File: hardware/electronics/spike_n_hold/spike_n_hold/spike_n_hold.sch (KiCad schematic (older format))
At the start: 132 parts, among them J1 input_trigger_2, J10 input_trigger_6, J11 input_trigger_5, J12 to_solenoid_6, J13 to_solenoid_5, J2 input_trigger_1, J3 to_solenoid_2, J4 to_solenoid_1, J5 input_trigger_4, J6 input_trigger_3, J7 to_solenoid_4, J8 to_solenoid_3, J9 Barrel_Jack_MountingPin, Q1 MJH11021G, Q10 MJH11021G, Q11 MPSA42, Q12 MPSA42, Q13 MPSA42, Q14 MPSA42, Q15 MJH11022G, Q16 MJH11022G, Q17 MJH11021G, Q18 MJH11021G, Q19 MPSA42, Q2 MJH11021G, Q20 MPSA42, Q21 MPSA42, Q22 MPSA42, Q23 MJH11022G, Q24 MJH11022G, Q3 MPSA42, Q4 MPSA42, Q5 MPSA42, Q6 MPSA42, Q7 MJH11022G, Q8 MJH11022G, Q9 MJH11021G, U1 LM555xM, U2 LM555xM, U3 LM555xM, U4 LM555xM, U5 LM2596T-12, U6 LM555xM, U7 LM555xM

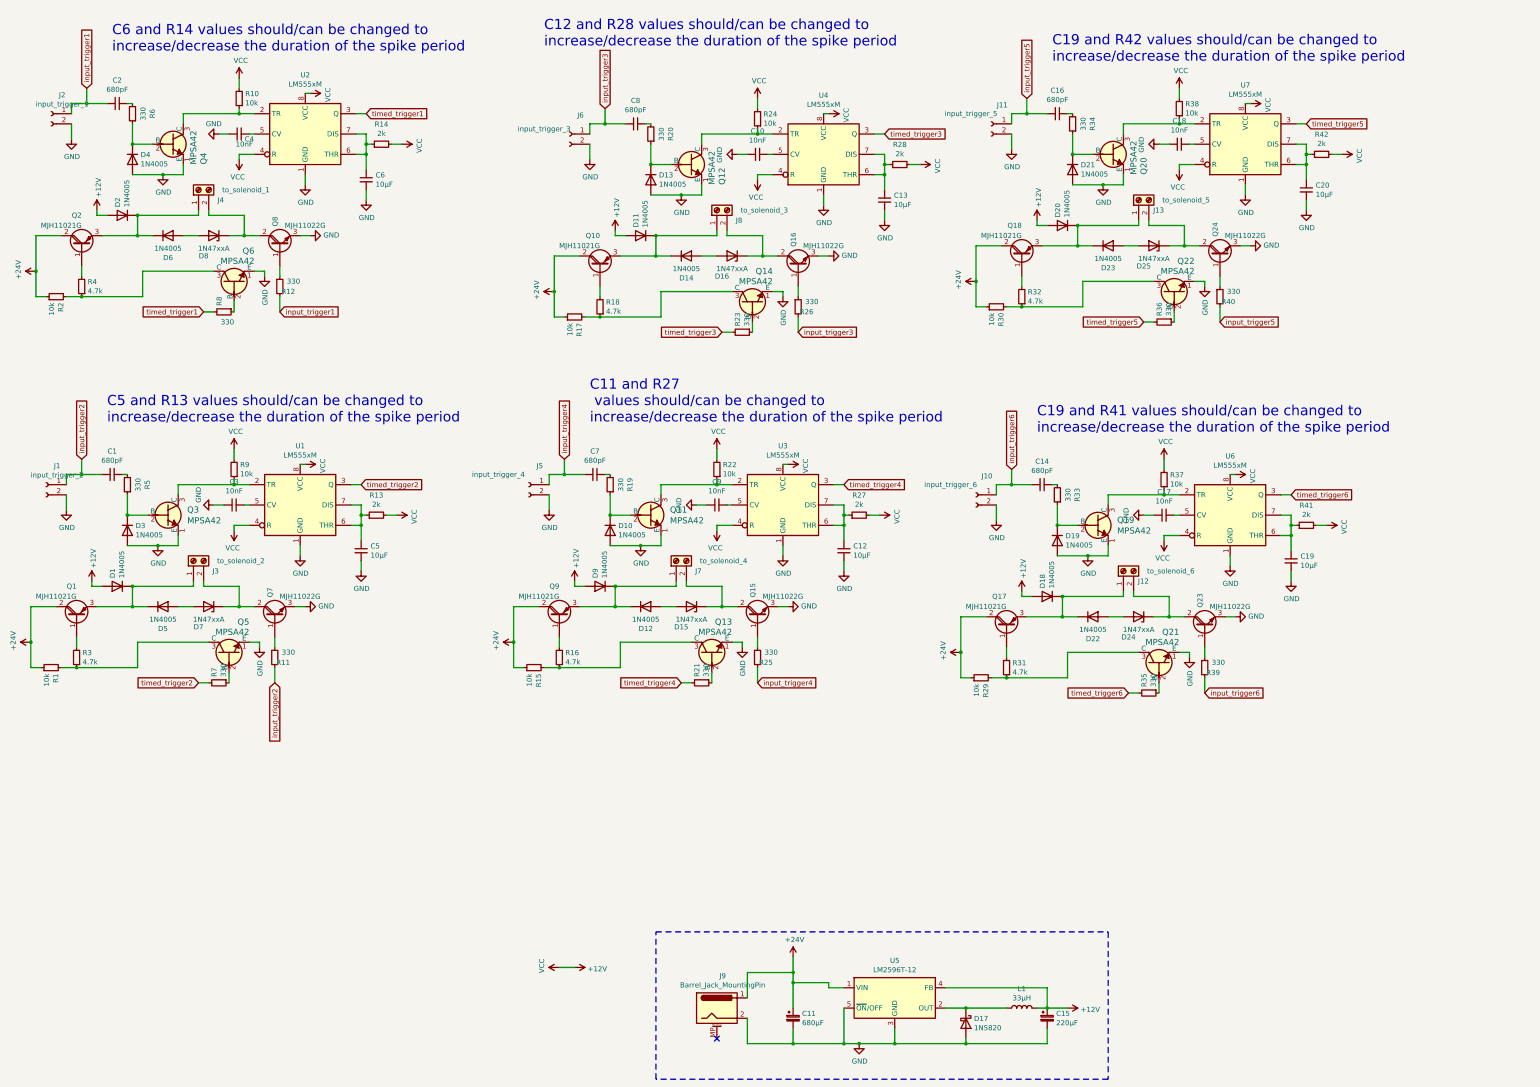
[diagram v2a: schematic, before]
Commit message: reimplementation, 2 modules per board, as they are equivalent to one odour channel, or one dilution step
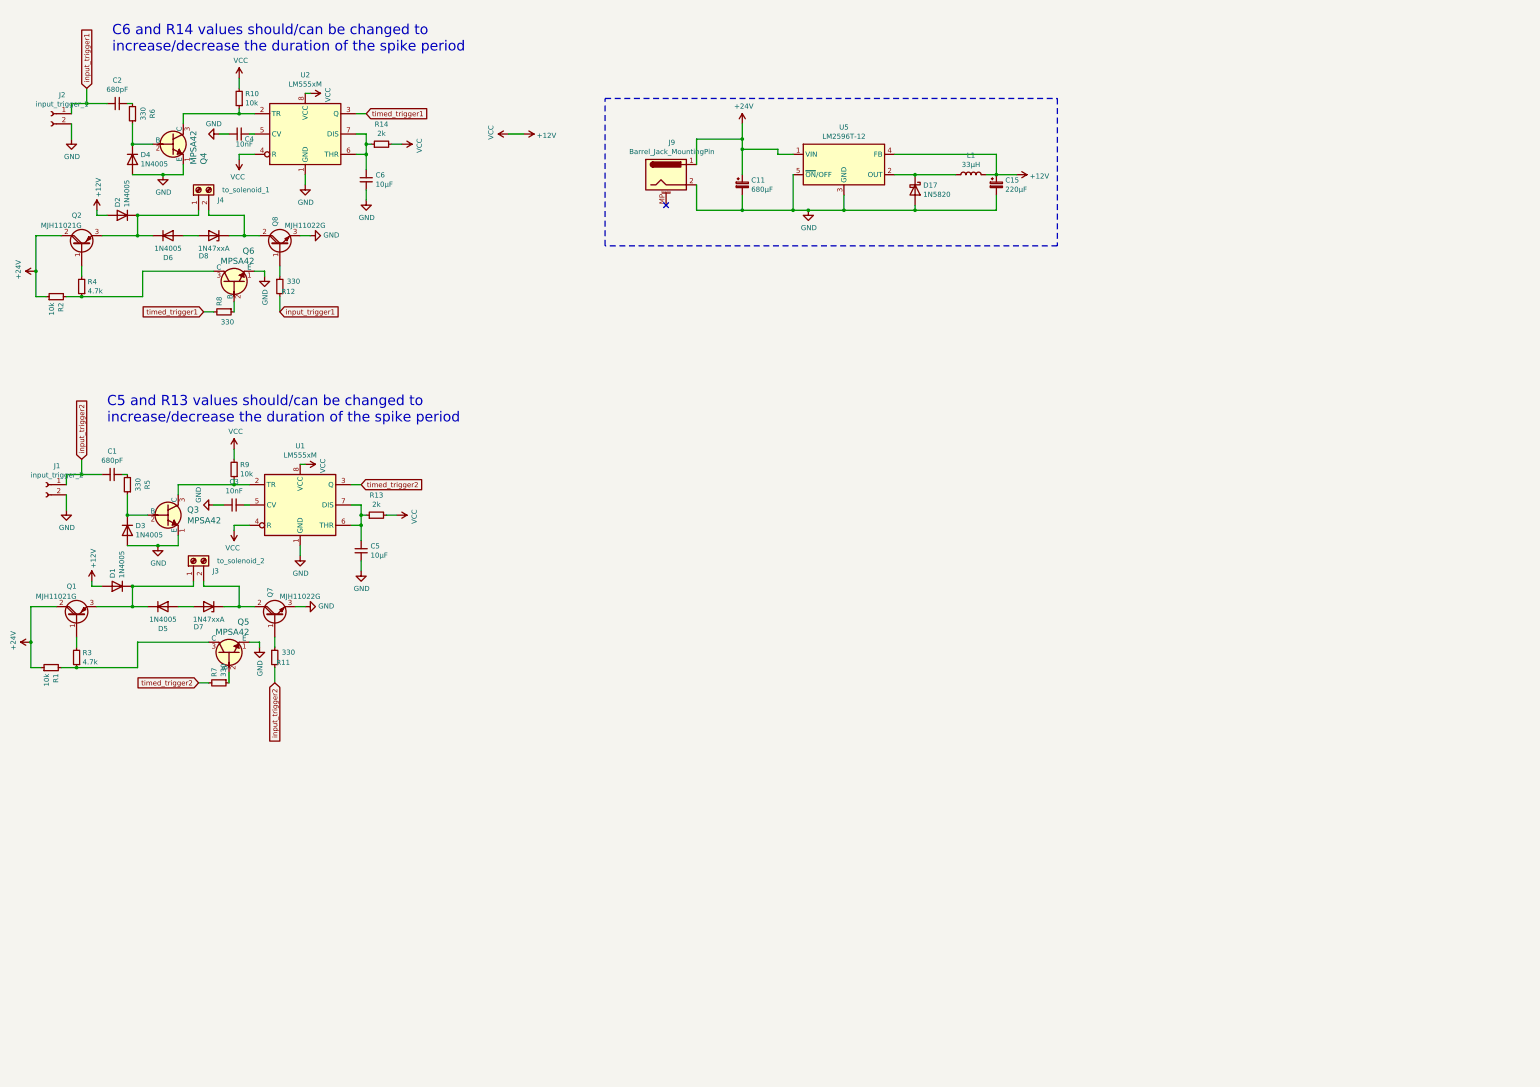
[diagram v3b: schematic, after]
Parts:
- removed C10, C17, C18, C9: 10nF, Capacitor_THT:C_Disc_D5.1mm_W3.2mm_P5.00mm, symbol Device:C_Small
- removed C12, C13, C19, C20: 10µF, Capacitor_THT:C_Disc_D5.1mm_W3.2mm_P5.00mm, symbol Device:C_Small
- removed C14, C16, C7, C8: 680pF, Capacitor_THT:C_Disc_D5.1mm_W3.2mm_P5.00mm, symbol Device:C_Small
- removed D10, D11, D12, D13, D14, D18, D19, D20, D21, D22, D23, D9: 1N4005, Diode_THT:D_DO-41_SOD81_P10.16mm_Horizontal, symbol Diode:1N4005
- removed D15, D16, D24, D25: 1N47xxA, Diode_THT:D_DO-41_SOD81_P10.16mm_Horizontal, symbol Diode:1N47xxA
- removed J10: input_trigger_6, Connector_PinHeader_2.54mm:PinHeader_1x02_P2.54mm_Vertical, symbol Connector:Conn_01x02_Female
- removed J11: input_trigger_5, Connector_PinHeader_2.54mm:PinHeader_1x02_P2.54mm_Vertical, symbol Connector:Conn_01x02_Female
- removed J12: to_solenoid_6, Connector_PinHeader_2.54mm:PinHeader_1x02_P2.54mm_Vertical, symbol Connector:Screw_Terminal_01x02
- removed J13: to_solenoid_5, Connector_PinHeader_2.54mm:PinHeader_1x02_P2.54mm_Vertical, symbol Connector:Screw_Terminal_01x02
- removed J5: input_trigger_4, Connector_PinHeader_2.54mm:PinHeader_1x02_P2.54mm_Vertical, symbol Connector:Conn_01x02_Female
- removed J6: input_trigger_3, Connector_PinHeader_2.54mm:PinHeader_1x02_P2.54mm_Vertical, symbol Connector:Conn_01x02_Female
- removed J7: to_solenoid_4, Connector_PinHeader_2.54mm:PinHeader_1x02_P2.54mm_Vertical, symbol Connector:Screw_Terminal_01x02
- removed J8: to_solenoid_3, Connector_PinHeader_2.54mm:PinHeader_1x02_P2.54mm_Vertical, symbol Connector:Screw_Terminal_01x02
- removed Q10, Q17, Q18, Q9: MJH11021G, Package_TO_SOT_THT:TO-247-3_Vertical, symbol Device:Q_PNP_Darlington_BCE
- removed Q11, Q12, Q13, Q14, Q19, Q20, Q21, Q22: MPSA42, Package_TO_SOT_THT:TO-92L_Inline_Wide, symbol dk_Transistors-Bipolar-BJT-Single:MPSA42
- removed Q15, Q16, Q23, Q24: MJH11022G, Package_TO_SOT_THT:TO-247-3_Vertical, symbol Device:Q_NPN_Darlington_BCE
- removed R15, R17, R22, R24, R29, R30, R37, R38: 10k, Resistor_THT:R_Axial_DIN0411_L9.9mm_D3.6mm_P12.70mm_Horizontal, symbol Device:R_Small
- removed R16, R18, R31, R32: 4.7k, Resistor_THT:R_Axial_DIN0411_L9.9mm_D3.6mm_P12.70mm_Horizontal, symbol Device:R_Small
- removed R19, R20, R21, R23, R25, R26, R33, R34, R35, R36, R39, R40: 330, Resistor_THT:R_Axial_DIN0411_L9.9mm_D3.6mm_P12.70mm_Horizontal, symbol Device:R_Small
- removed R27, R28, R41, R42: 2k, Resistor_THT:R_Axial_DIN0411_L9.9mm_D3.6mm_P12.70mm_Horizontal, symbol Device:R_Small
- removed U3, U4, U6, U7: LM555xM, Package_DIP:DIP-8_W7.62mm_LongPads, symbol Timer:LM555xM
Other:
- note removed: "C11 and R27\n values should/can be changed to\nincrease/decrease the duration of the spike period"
- note removed: "C12 and R28 values should/can be changed to\nincrease/decrease the duration of the spike period"
- note removed: "C19 and R41 values should/can be changed to\nincrease/decrease the duration of the spike period"
- note removed: "C19 and R42 values should/can be changed to\nincrease/decrease the duration of the spike period"
- moved on the sheet: C11, C15, D17, J9, L1, U5
